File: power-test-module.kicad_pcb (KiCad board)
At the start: 2 copper layers, 38.4 x 23.9 mm, 43 parts, among them J1 USB_miniB, J2 USB_C_Receptacle, J3 Conn_01x06, J4 Conn_01x06, U1 USB3740B-AI9, U2 UTC2000, U3 FT232RL, U4 74LVC1G00, U5 SC185

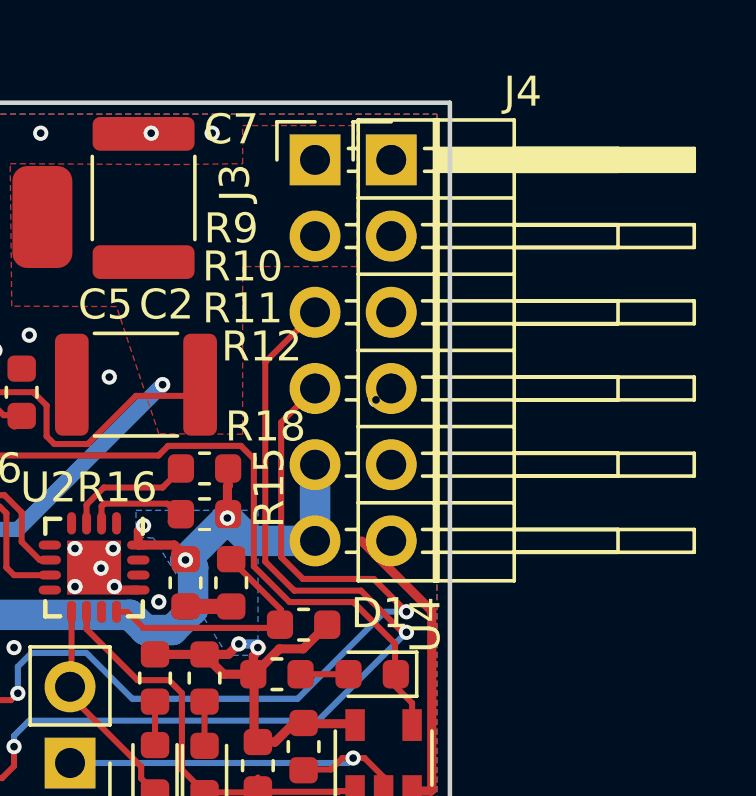
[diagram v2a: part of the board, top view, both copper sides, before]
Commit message: fixed design-rule issues
 - removed stray via
 - replaced 2 single-row headers by a 2x6 (vertical) header to
   avoid court-yard overlaps.
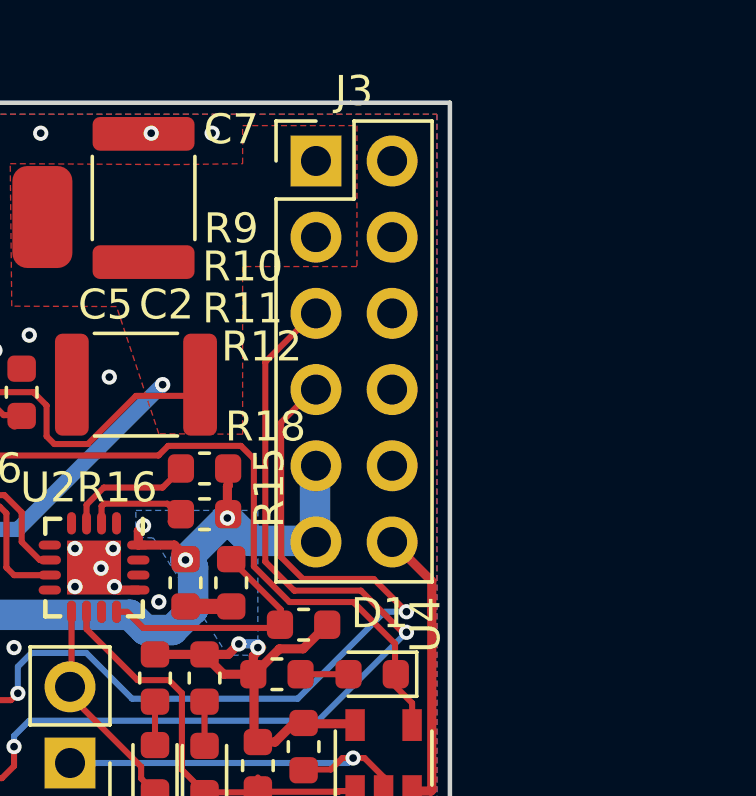
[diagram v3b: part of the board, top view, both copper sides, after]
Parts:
- removed J4: Conn_01x06, Connector_PinHeader_2.54mm:PinHeader_1x06_P2.54mm_Horizontal
- J3: value Conn_01x06 -> Conn_02x06_Odd_Even; footprint Connector_PinHeader_2.54mm:PinHeader_1x06_P2.54mm_Horizontal -> Connector_PinHeader_2.54mm:PinHeader_2x06_P2.54mm_Vertical
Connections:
- J3 pad 2: +3V3 -> GND
- J3 pad 3: UART_RX_MIO14 -> +3V3
- J3 pad 4: UART_TX_MIO15 -> GND
- J3 pad 5: +5V -> UART_RX_MIO14
- J3 pad 6: +5V -> GND
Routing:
- net GND: track 45.6 -> 45.2 mm, vias 44 -> 43

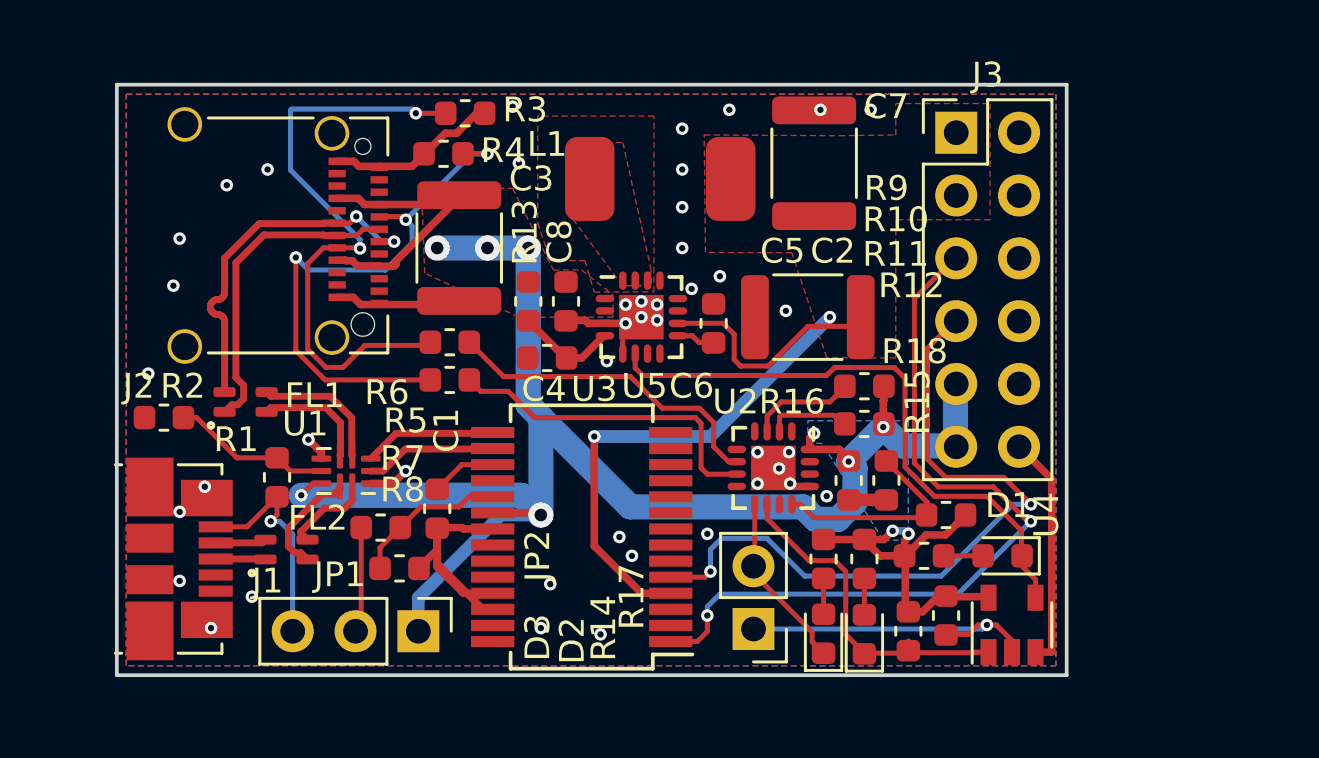
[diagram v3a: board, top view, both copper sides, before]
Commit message: re-annotated with base number 1000
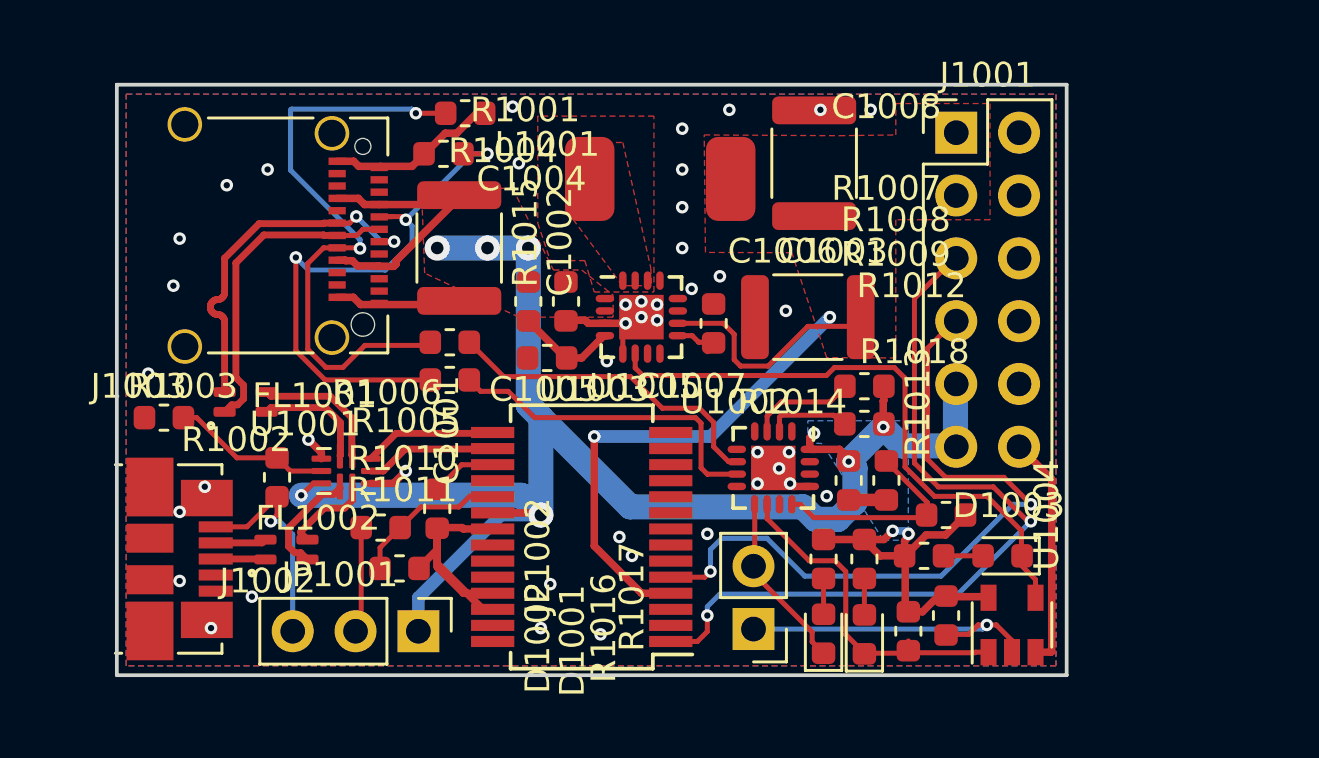
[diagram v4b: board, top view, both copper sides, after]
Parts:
- renumbered C1 to C1001, C8 to C1002, C2 to C1003, C3 to C1004, C4 to C1005, C5 to C1006, C6 to C1007, C7 to C1008, D2 to D1001, D3 to D1002, D1 to D1003, FL1 to FL1001, FL2 to FL1002, J3 to J1001, J1 to J1002, J2 to J1003, JP1 to JP1001, JP2 to JP1002, L1 to L1001, R3 to R1001, R1 to R1002, R2 to R1003, R4 to R1004, R5 to R1005, R6 to R1006, R9 to R1007, R10 to R1008, R11 to R1009, R7 to R1010, R8 to R1011, R12 to R1012, R15 to R1013, R16 to R1014, R13 to R1015, R14 to R1016, R17 to R1017, R18 to R1018, U1 to U1001, U2 to U1002, U3 to U1003, U4 to U1004, U5 to U1005

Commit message: use hierarchical labels from power-and-uart sheet
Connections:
- net USB_C_D_N renamed /Sheet5C4CE702/USB_C_D_N
- net USB_C_D_P renamed /Sheet5C4CE702/USB_C_D_P

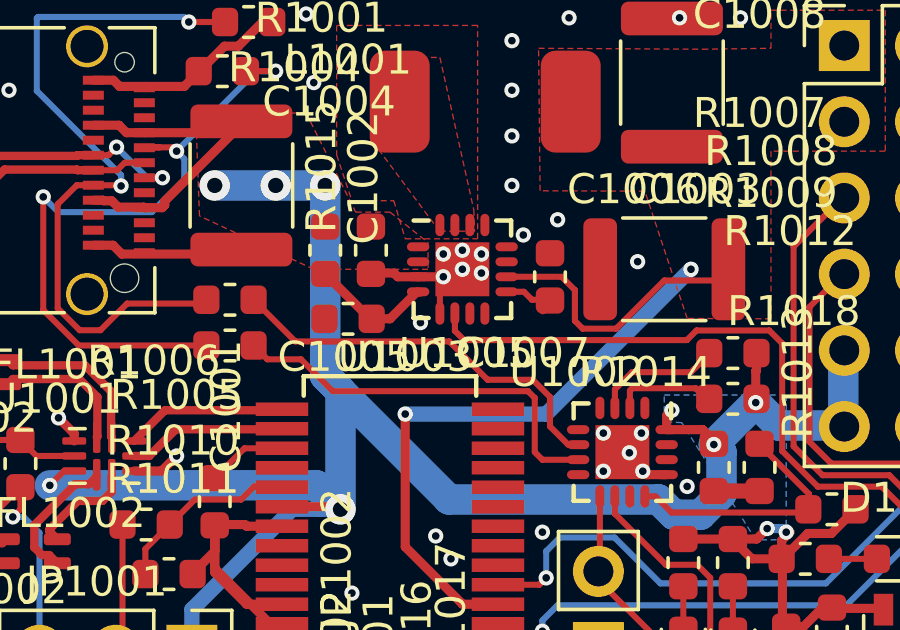
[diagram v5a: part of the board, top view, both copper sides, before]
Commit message: use QFN-16 footprint from proj-library
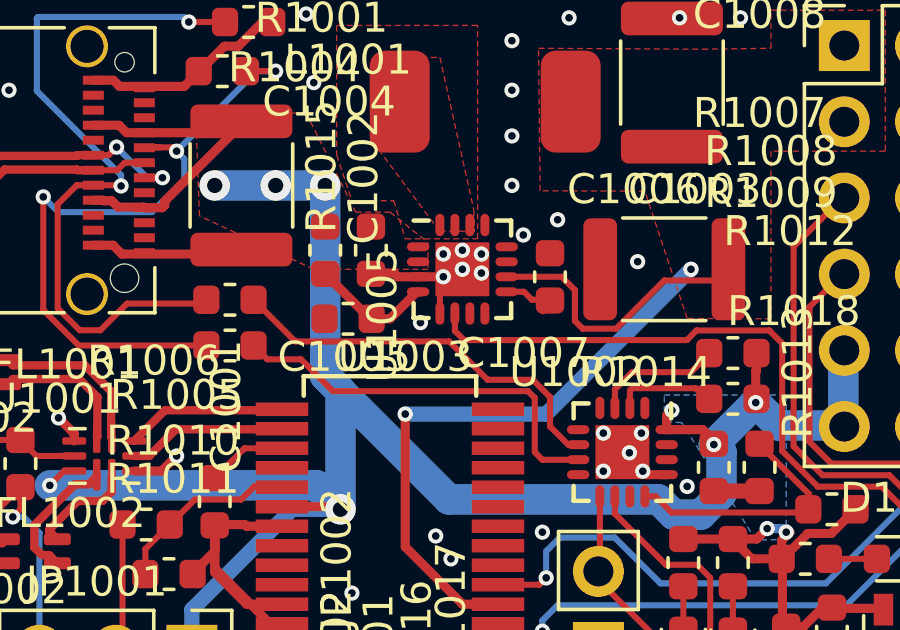
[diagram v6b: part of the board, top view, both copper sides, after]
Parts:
- U1002, U1005: footprint Package_DFN_QFN:QFN-16-1EP_3x3mm_P0.5mm_EP1.8x1.8mm -> proj_footprints:QFN-16-1EP_3x3mm_P0.5mm_EP1.8x1.8mm

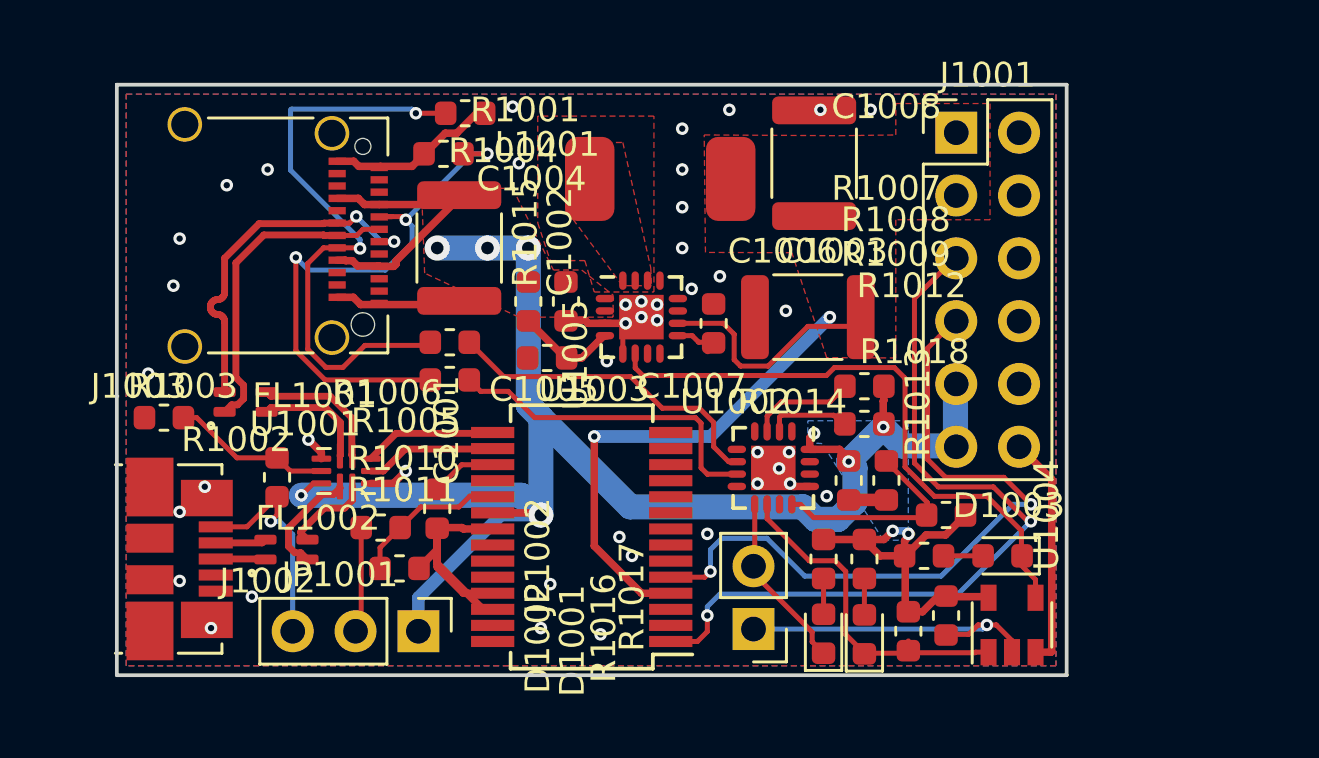
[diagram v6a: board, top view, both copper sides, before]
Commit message: swapped USBC connector; jlcpcb hole distance.
- use usbc-usb2.0 variant with more power pins
- enforce .5mm hole spacing (jlcpcb)
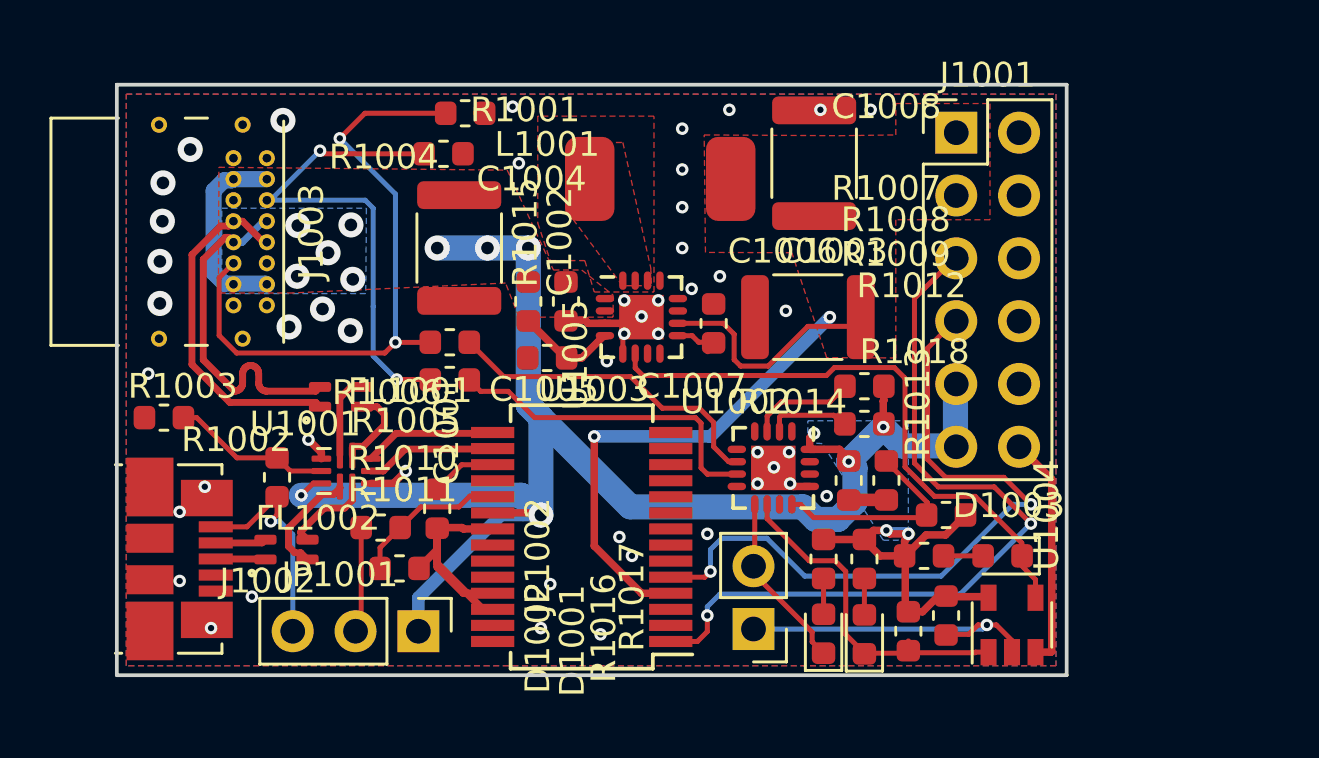
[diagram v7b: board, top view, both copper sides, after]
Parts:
- J1003: value USB_C_Receptacle -> USB_C_Receptacle_USB2.0; footprint Connector_USB:USB_C_Receptacle_Amphenol_12401610E4-2A_CircularHoles -> proj_footprints:USB_C_Receptacle_GCT_USB4085_smaller_holes
- moved FL1001 3.86 mm to (122.3, 125.7)
- moved J1003 3.16 mm to (119.3, 116.0)
- turned R1004 to 0 degrees
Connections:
- FL1001 pad 1: /Sheet5C4CE702/USB_C_D_P -> /Sheet5C4CE702/USB_C_D_N
- FL1001 pad 2: /Sheet5C4CE702/USB1_P -> /Sheet5C4CE702/USB1_N
- FL1001 pad 3: /Sheet5C4CE702/USB1_N -> /Sheet5C4CE702/USB1_P
- FL1001 pad 4: /Sheet5C4CE702/USB_C_D_N -> /Sheet5C4CE702/USB_C_D_P
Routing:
- net GND: track 45.2 -> 33.3 mm, vias 43 -> 47
- net Net-(J1003-PadA5): track 23.2 -> 20.2 mm, vias 3 -> 2
- net /Sheet5C4CE702/USB1_N: track 5.41 -> 3.47 mm
- net +5V: track 90.5 -> 88.6 mm, vias 10 -> 15
- net Net-(J1003-PadB5): track 24.7 -> 26.0 mm
- net /Sheet5C4CE702/USB_C_D_P: track 13.0 -> 14.3 mm
- net /Sheet5C4CE702/USB1_P: track 4.65 -> 3.39 mm
- net /Sheet5C4CE702/USB_C_D_N: track 14.6 -> 14.3 mm, vias 2 -> 0
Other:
- net class Default: clearance 0.1778 -> 0.1524
- rule trace_clearance: 0.1778 -> 0.1524

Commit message: use special +5/+3V3 labels with more specific net names
This allows easier integration since these are global labels
and using more specific names helps avoiding clashes.

The labels are stored in the 'rescue' library.

Strangely: the same trick did not work for GND. Kicad always
insists the net name remains 'GND' (it does work, however if
a new schematic is created - then the different net name for
GND 'sticks').
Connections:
- net +3V3 renamed +3V3_PWR_OUT
- net +5V renamed +5V_PWR_OUT
